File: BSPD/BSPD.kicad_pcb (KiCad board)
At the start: 2 copper layers, 81 x 61 mm, 31 parts, among them Q101 Q_PMOS_GSD, U101 641964-1, U102 641964-1, U103 R-78E5.0-0.5, U104 SN74LVC1G08DBVR, U105 LM339DR, U106 NE555DR, U107 SN74LVC3G14DCUR, U108 SN74AC32DR, U109 SN74LVC1G08DBVR, U110 641964-1

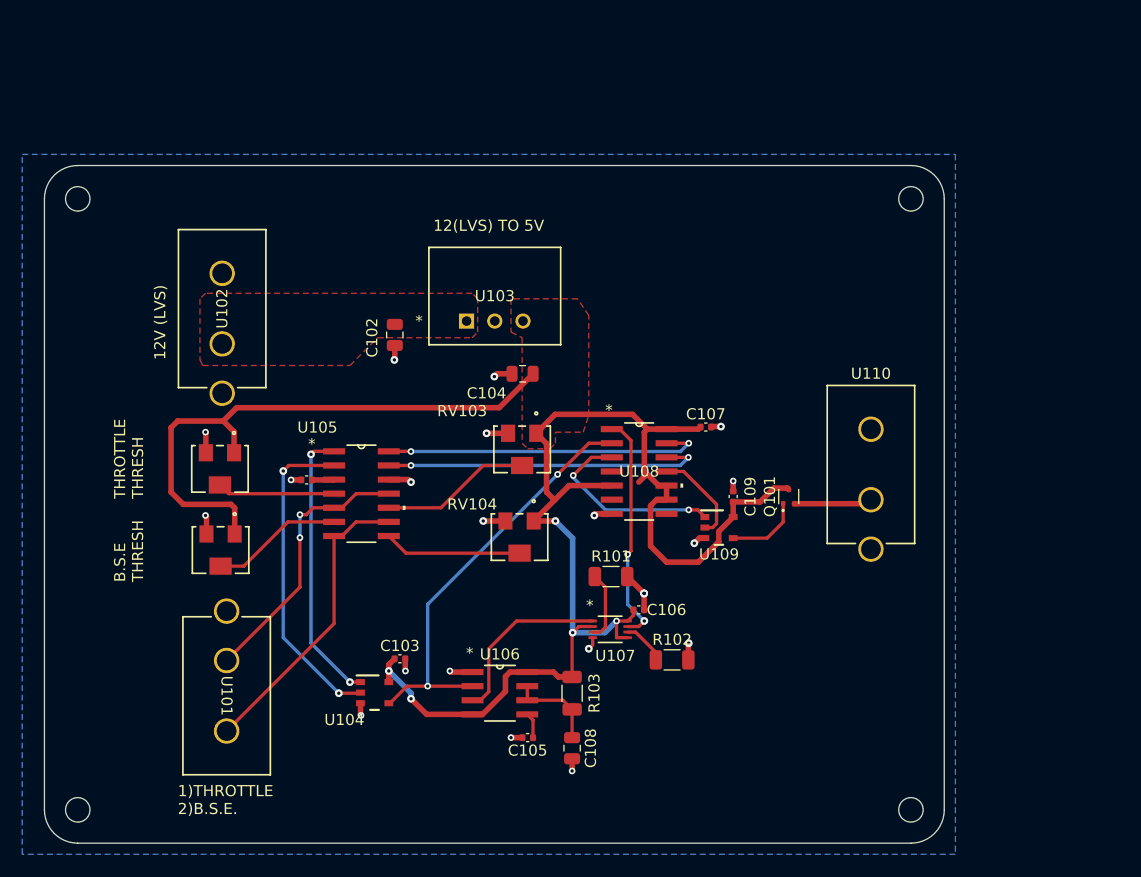
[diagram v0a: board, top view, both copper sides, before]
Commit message: resolved DRC errors for via sizes and footprints.
via size changed to 6mm/3mm should still work for JLC. Connected unconnected items. Changed footprints to fix overlap issue
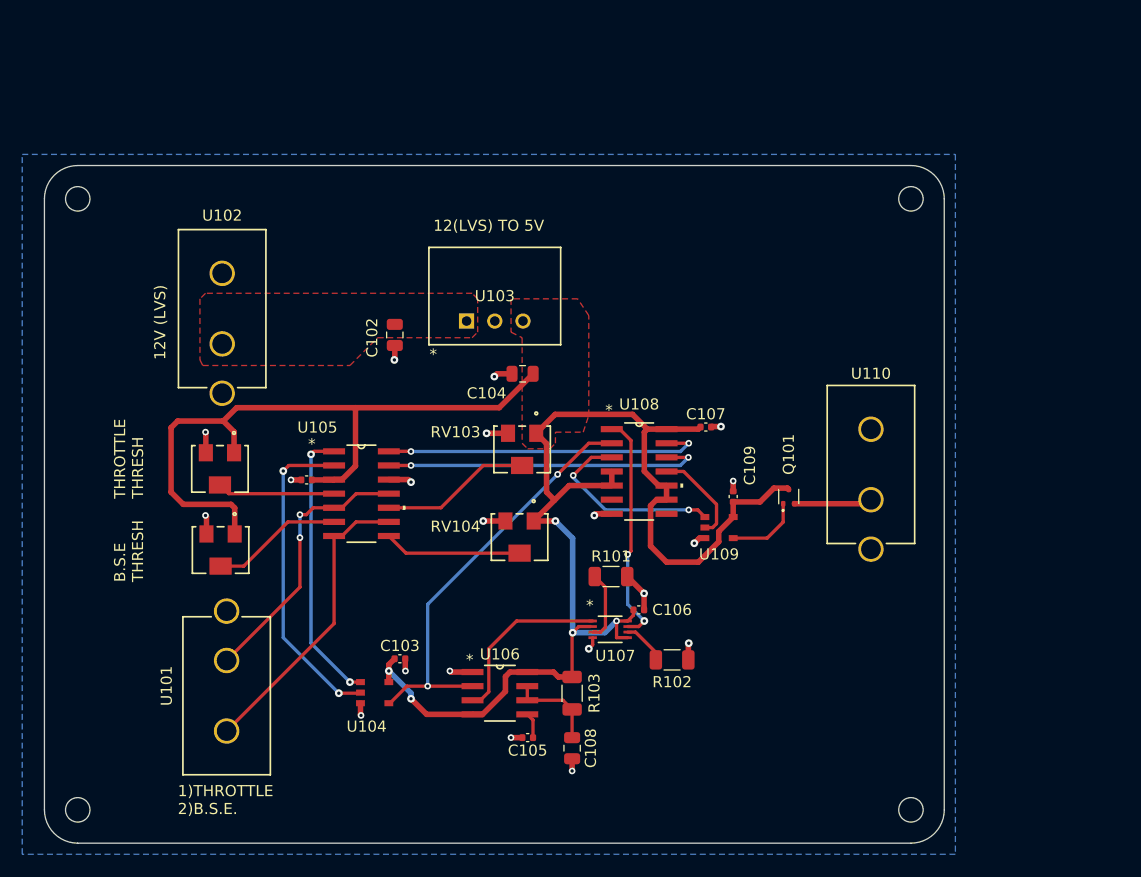
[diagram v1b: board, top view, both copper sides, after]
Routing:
- net +5V: track 167.8 -> 175.5 mm
- net GND: vias 21 -> 20
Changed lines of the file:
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@@
 		)
 		(fp_text user "*"
-			(at -2.7178 -3.6068 0)
-			(unlocked yes)
-			(layer "F.SilkS")
-			(effects
-				(font
-					(size 1 1)
-					(thickness 0.15)
-				)
-			)
-		)
-		(fp_text user "*"
-			(at -2.7178 -3.6068 0)
+			(at -2.7178 -3 0)
 			(layer "F.SilkS")
 			(effects
@@
 		(tags "SOT-523")
 		(property "Reference" "Q101"
-			(at 0 -1.7 90)
+			(at 3.8 0 90)
 			(layer "F.SilkS")
 			(effects
@@
 		(tags "641964-1 ")
 		(property "Reference" "U102"
-			(at 3.175 0 90)
+			(at 11.555 0 0)
 			(unlocked yes)
 			(layer "F.SilkS")
@@
 		(tags "3224W-1-103E ")
 		(property "Reference" "RV103"
-			(at 5.4 3.4522 0)
+			(at 6 1.5522 0)
 			(unlocked yes)
 			(layer "F.SilkS")
@@
 		(tags "resistor")
 		(property "Reference" "R102"
-			(at 0 -1.82 0)
+			(at 0 1.999999 0)
 			(layer "F.SilkS")
 			(effects
@@
 		(tags "capacitor")
 		(property "Reference" "C109"
-			(at 0 1.54 90)
+			(at 2.8 1.5 90)
 			(layer "F.SilkS")
 			(effects
@@
 		(tags "capacitor")
 		(property "Reference" "C106"
-			(at 2.5 0 0)
+			(at 3 0 0)
 			(layer "F.SilkS")
 			(effects
@@
 		(tags "SN74LVC1G08DBVR ")
 		(property "Reference" "U104"
-			(at -2.725001 2.449998 0)
+			(at -0.725001 3.049999 0)
 			(unlocked yes)
 			(layer "F.SilkS")
@@
 		(attr smd)
 		(fp_line
-			(start -1.625001 -1.549999)
-			(end 0.349999 -1.549999)
-			(stroke
-				(width 0.2)
-				(type solid)
-			)
-			(layer "F.SilkS")
-		)
-		(fp_line
-			(start -0.399999 1.549999)
-			(end 0.375003 1.549999)
-			(stroke
-				(width 0.2)
-				(type solid)
-			)
-			(layer "F.SilkS")
-		)
-		(fp_line
 			(start -1.750002 -1.650002)
 			(end 1.749999 -1.650002)
@@
 		)
 		(fp_line
-			(start -0.500002 0)
-			(end 0.499999 0)
-			(stroke
-				(width 0.1)
-				(type solid)
-			)
-			(layer "F.CrtYd")
-		)
-		(fp_line
-			(start 0 0.499999)
-			(end 0 -0.500002)
-			(stroke
-				(width 0.1)
-				(type solid)
-			)
-			(layer "F.CrtYd")
-		)
-		(fp_line
 			(start 1.749999 1.649999)
 			(end 1.749999 -1.650002)
@@
 		)
 		(fp_text user "*"
-			(at -4.2799 0 0)
-			(unlocked yes)
-			(layer "F.SilkS")
-			(effects
-				(font
-					(size 1 1)
-					(thickness 0.15)
-				)
-			)
-		)
-		(fp_text user "*"
-			(at -4.2799 0 0)
+			(at -3 3 0)
 			(layer "F.SilkS")
 			(effects
@@
 		(tags "SN74AC32DR ")
 		(property "Reference" "U108"
-			(at 0 0 0)
+			(at 0 -6.04 0)
 			(unlocked yes)
 			(layer "F.SilkS")
@@
 		(fp_text user "*"
 			(at -2.7178 -5.5118 0)
-			(layer "F.SilkS")
-			(effects
-				(font
-					(size 1 1)
-					(thickness 0.15)
-				)
-			)
-		)
-		(fp_text user "*"
-			(at -2.7178 -5.5118 0)
 			(unlocked yes)
 			(layer "F.SilkS")
@@
 		(tags "641964-1 ")
 		(property "Reference" "U101"
-			(at 3.175 0 270)
+			(at 2.286 5.4 90)
 			(unlocked yes)
 			(layer "F.SilkS")
@@
 		(attr smd)
 		(fp_line
-			(start -1.625001 -1.549999)
-			(end 0.349999 -1.549999)
-			(stroke
-				(width 0.2)
-				(type solid)
-			)
-			(layer "F.SilkS")
-		)
-		(fp_line
-			(start -0.399999 1.549999)
-			(end 0.375003 1.549999)
-			(stroke
-				(width 0.2)
-				(type solid)
-			)
-			(layer "F.SilkS")
-		)
-		(fp_line
 			(start -1.750002 -1.650002)
 			(end 1.749999 -1.650002)
@@
 		)
 		(fp_line
-			(start -0.500002 0)
-			(end 0.499999 0)
-			(stroke
-				(width 0.1)
-				(type solid)
-			)
-			(layer "F.CrtYd")
-		)
-		(fp_line
-			(start 0 0.499999)
-			(end 0 -0.500002)
-			(stroke
-				(width 0.1)
-				(type solid)
-			)
-			(layer "F.CrtYd")
-		)
-		(fp_line
 			(start 1.749999 1.649999)
 			(end 1.749999 -1.650002)
@@
 		)
 		(fp_text user "*"
-			(at -1.8288 -2.147 0)
-			(unlocked yes)
-			(layer "F.SilkS")
-			(effects
-				(font
-					(size 1 1)
-					(thickness 0.15)
-				)
-			)
-		)
-		(fp_text user "*"
 			(at -0.8128 -0.9779 0)
 			(layer "F.Fab")
@@
 		(tags "3224W-1-103E ")
 		(property "Reference" "RV104"
-			(at 4.27 2.9478 0)
+			(at 5.77 0.9478 0)
 			(unlocked yes)
 			(layer "F.SilkS")
@@
 	)
 	(via
-		(at 159.98 125.517501)
-		(size 0.7)
-		(drill 0.3)
-		(layers "F.Cu" "B.Cu")
-		(net 2)
-	)
-	(via
 		(at 164 130)
 		(size 0.7)
@@
 	)
 	(segment
+		(start 134 108.8)
+		(end 146.940068 108.8)
+		(width 0.5)
+		(layer "F.Cu")
+		(net 3)
+	)
+	(segment
 		(start 164.8662 110.73)
 		(end 165.0562 110.54)
@@
 	)
 	(segment
+		(start 157.0724 114.54)
+		(end 157.0724 115.81)
+		(width 0.5)
+		(layer "F.Cu")
+		(net 3)
+	)
+	(segment
 		(start 122.8 117.5)
 		(end 123.127597 117.827597)
@@
 	)
 	(segment
+		(start 134 114.0536)
+		(end 134 108.8)
+		(width 0.5)
+		(layer "F.Cu")
+		(net 3)
+	)
+	(segment
 		(start 117.4 116.4)
 		(end 118.5 117.5)
@@
 	)
 	(segment
-		(start 160 115)
-		(end 159.5 115.5)
-		(width 0.5)
-		(layer "F.Cu")
-		(net 3)
-	)
-	(segment
 		(start 132.0424 115.3)
 		(end 132.0724 115.27)
@@
 	)
 	(segment
+		(start 132.0724 115.27)
+		(end 132.7836 115.27)
+		(width 0.5)
+		(layer "F.Cu")
+		(net 3)
+	)
+	(segment
 		(start 147.5 134.3432)
 		(end 147.5 133)
@@
 	)
 	(segment
-		(start 160 114.5212)
-		(end 160 115)
-		(width 0.5)
-		(layer "F.Cu")
-		(net 3)
-	)
-	(segment
 		(start 117.4 110.6)
 		(end 117.4 116.4)
@@
 	)
 	(segment
+		(start 132.7836 115.27)
+		(end 134 114.0536)
+		(width 0.5)
+		(layer "F.Cu")
+		(net 3)
+	)
+	(segment
 		(start 160.27 110.73)
 		(end 162 110.73)
@@
 	(segment
 		(start 123.3 108.8)
-		(end 146.940068 108.8)
+		(end 134 108.8)
 		(width 0.5)
 		(layer "F.Cu")

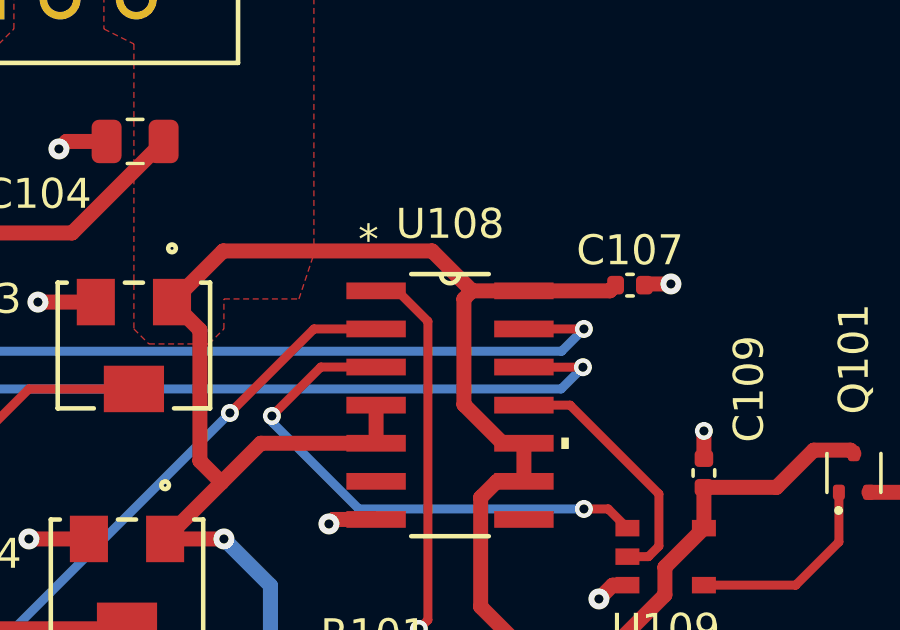
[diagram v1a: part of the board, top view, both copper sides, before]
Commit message: BSPD needs to be fixed + Fault Latch Layout Issue
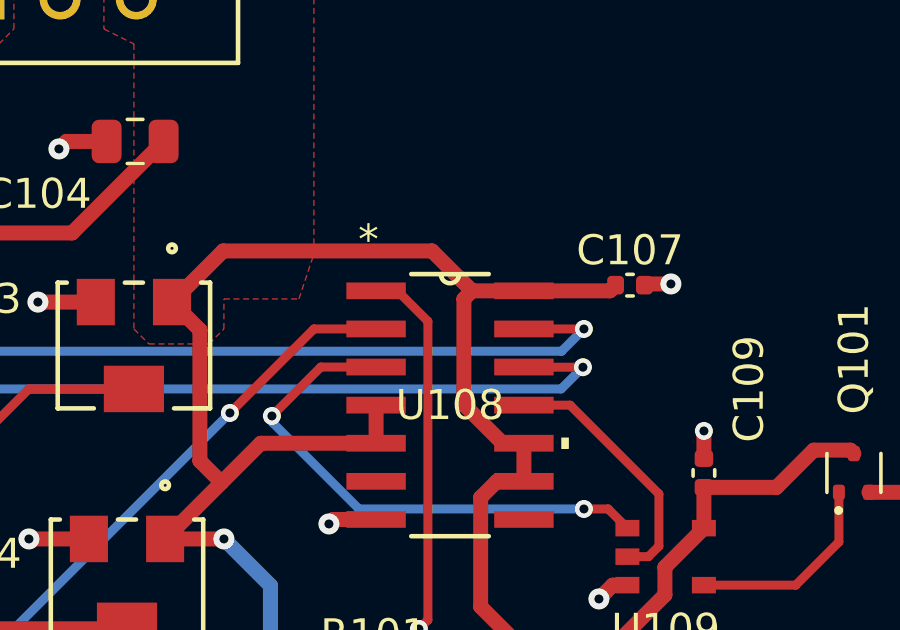
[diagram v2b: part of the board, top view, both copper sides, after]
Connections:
- Q101 pad 2: BSPD_TO_FAULT -> +5V
- Q101 pad 3: +5V -> BSPD_TO_FAULT
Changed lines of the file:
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@@
 			(layers "F.Cu" "F.Mask" "F.Paste")
 			(roundrect_rratio 0.25)
-			(net 6 "BSPD_TO_FAULT")
+			(net 3 "+5V")
 			(pinfunction "S")
 			(pintype "passive")
@@
 			(layers "F.Cu" "F.Mask" "F.Paste")
 			(roundrect_rratio 0.25)
-			(net 3 "+5V")
+			(net 6 "BSPD_TO_FAULT")
 			(pinfunction "D")
 			(pintype "passive")
@@
 		(tags "SN74AC32DR ")
 		(property "Reference" "U108"
-			(at 0 -6.04 0)
+			(at 0 0 0)
 			(unlocked yes)
 			(layer "F.SilkS")
@@
 		(fp_text user "*"
 			(at -2.7178 -5.5118 0)
-			(unlocked yes)
 			(layer "F.SilkS")
 			(effects
@@
 			(at -2.7178 -5.5118 0)
 			(unlocked yes)
-			(layer "F.Fab")
+			(layer "F.SilkS")
 			(effects
 				(font
@@
 			(unlocked yes)
 			(layer "F.Fab")
+			(effects
+				(font
+					(size 1 1)
+					(thickness 0.15)
+				)
+			)
+		)
+		(fp_text user "*"
+			(at -2.7178 -5.5118 0)
+			(unlocked yes)
+			(layer "F.Fab")

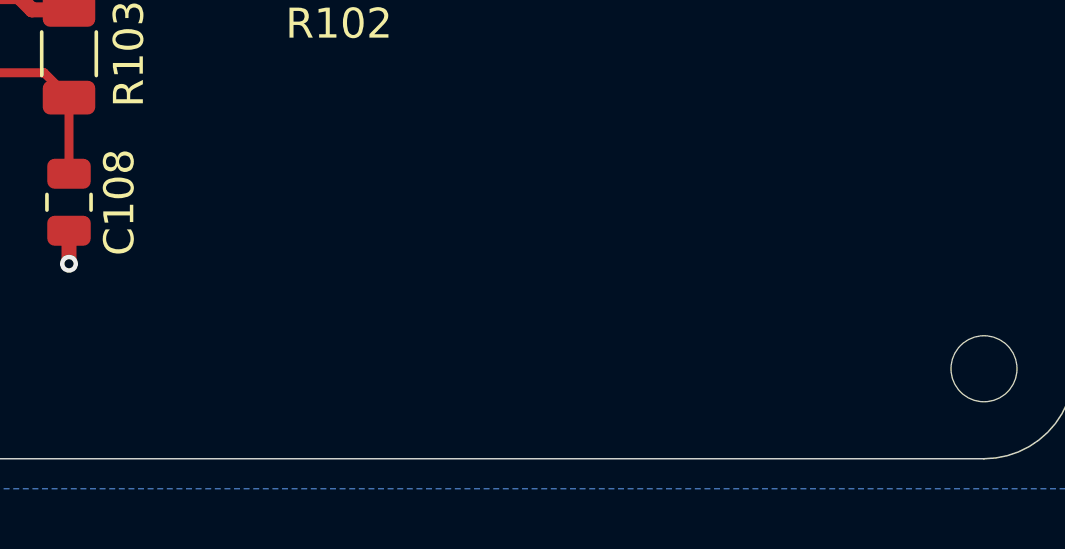
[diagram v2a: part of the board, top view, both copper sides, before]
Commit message: Fault latch added Logo
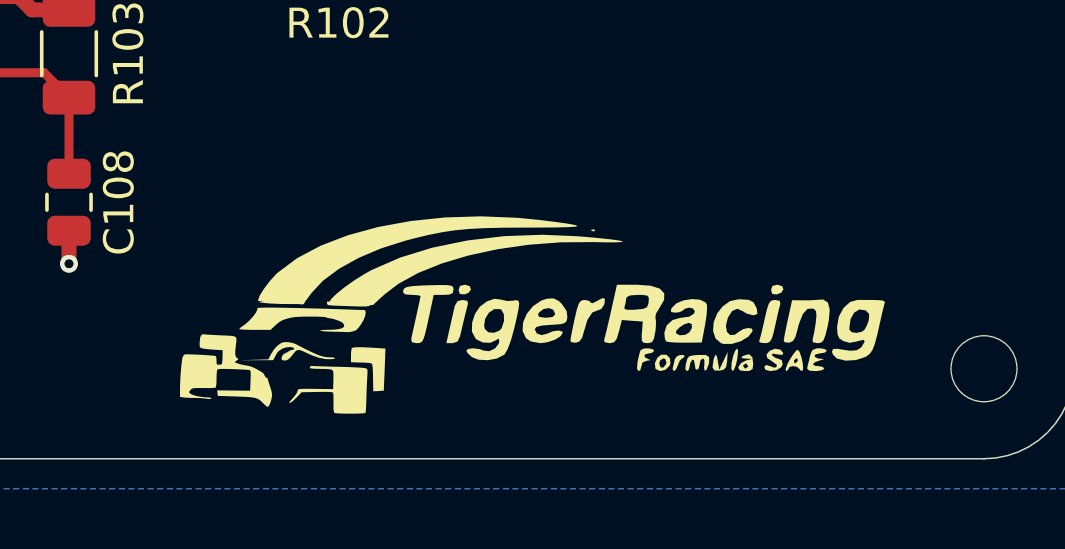
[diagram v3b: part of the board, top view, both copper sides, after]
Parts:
- added G***: LOGO, LOGO, F.Cu at (160.7, 144.7)
- added G***: LOGO, LOGO, F.Cu at (168.9, 143.3)

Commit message: BSPD READY
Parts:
- moved U107 18.9 mm to (171.6, 116.8)
- moved H101 18.9 mm to (123.7, 78.1)
- moved H102 18.9 mm to (123.7, 133.1)
- moved U104 18.9 mm to (150.4, 122.6)
- moved U109 18.9 mm to (181.4, 107.7)
- moved G*** 18.9 mm to (175.4, 132.8)
- moved RV102 18.9 mm to (136.5, 102.4)
- moved C105 18.9 mm to (164.2, 126.6)
- moved G*** 18.9 mm to (183.6, 131.4)
- moved H103 18.9 mm to (198.7, 133.1)
- moved H104 18.9 mm to (198.7, 78.1)
- moved R103 18.9 mm to (168.2, 122.6)
- moved RV101 18.9 mm to (136.6, 109.7)
- moved RV104 18.9 mm to (163.5, 108.5)
- moved U102 18.9 mm to (136.7, 91.2)
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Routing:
- net 2OUT: track 28.8 -> 85.9 mm, vias 2 -> 0
- net 1OUT: track 25.1 -> 74.9 mm, vias 2 -> 0
- net +5V: track 175.5 -> 224.1 mm, vias 5 -> 2
- net GND: track 30.8 -> 2.36 mm, vias 20 -> 289
- net THRESH_BSE: track 11.9 -> 37.8 mm
- net Net-(U108-1Y): track 17.7 -> 28.4 mm
- net BSE_IN: track 27.0 -> 17.3 mm
- net THRESH_THROTTLE: track 10.6 -> 14.2 mm
- net 3OUT: track 29.3 -> 31.9 mm, vias 2 -> 0
- net 4OUT: track 29.2 -> 31.6 mm, vias 2 -> 0
- net Net-(Q101-G): track 6.75 -> 5.23 mm
- net THROTTLE_IN: track 24.6 -> 23.2 mm, vias 2 -> 0
- net Net-(U104-Y): track 38.1 -> 39.5 mm, vias 2 -> 0
- net Net-(U106-OUT): track 16.7 -> 15.4 mm
- net BSPD_TO_FAULT: track 7.05 -> 8.05 mm
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- added copper zone on F.Cu, net GND
- removed copper zone on F.Cu, net +5V

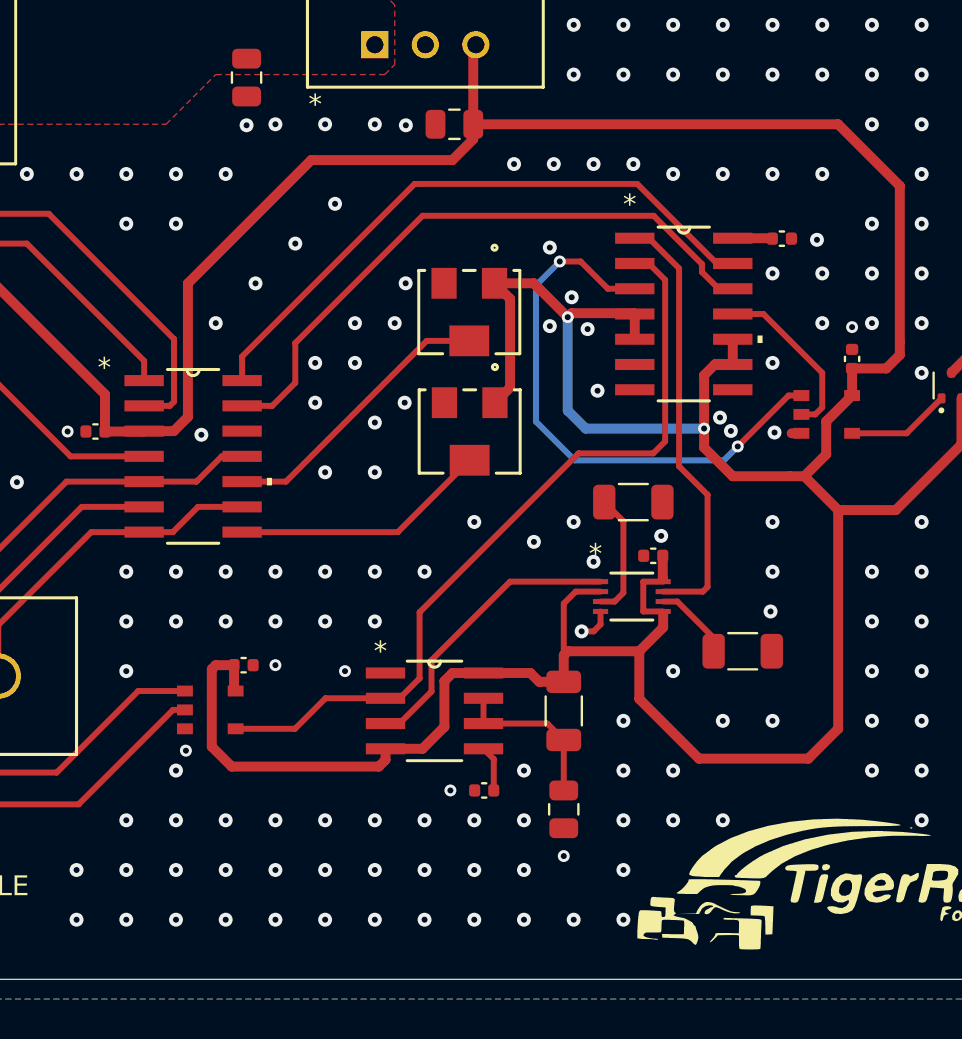
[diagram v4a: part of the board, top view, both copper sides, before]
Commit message: Double checked PMOS output logic. Added connector and routing for sense wires from sensors. Connected one unconnected track. 2 DRC errors about spokes, but otherwise Ready to Geaux :3
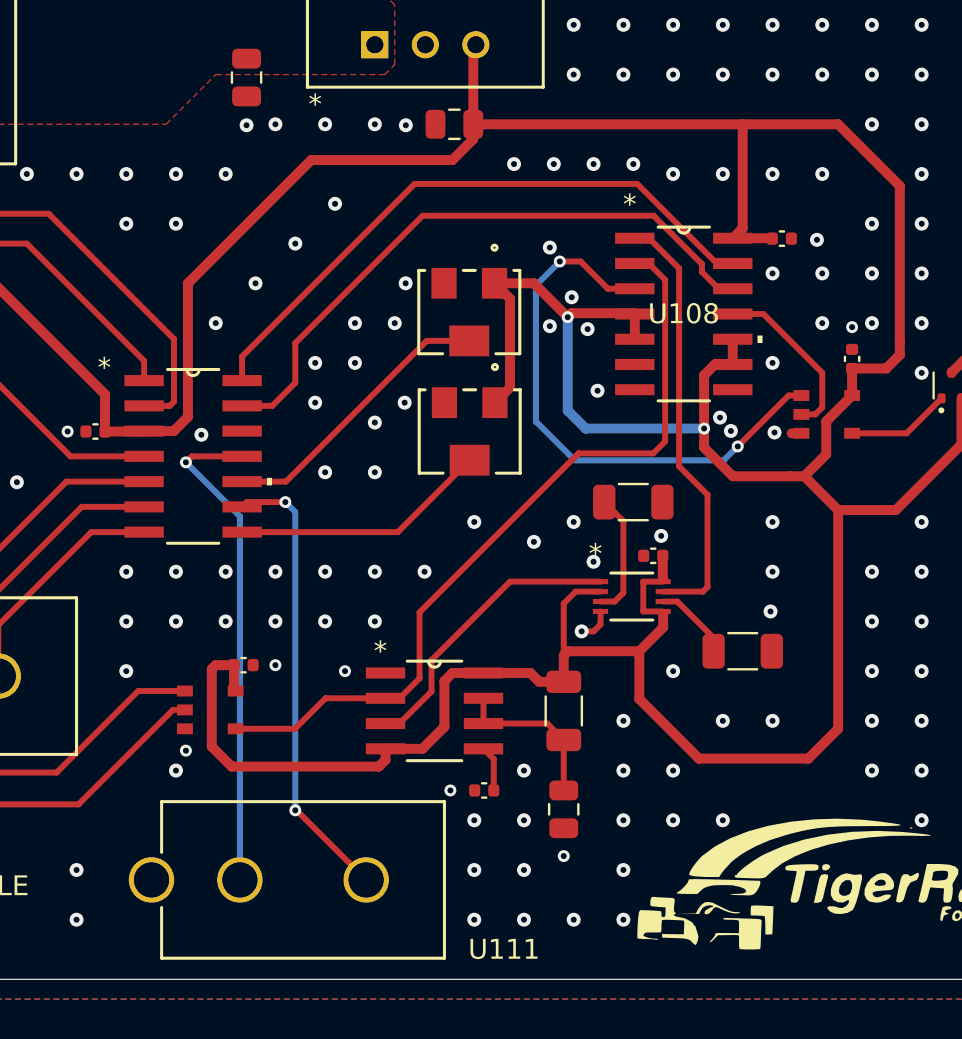
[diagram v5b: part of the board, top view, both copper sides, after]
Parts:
- added U111: 641964-1, 641964-1:641964-1_TYC, F.Cu at (151.9, 131.1)
- U108: footprint SN74AC32DR:D14 -> LM339DR:D14
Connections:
- U105 pad 11: THROTTLE_IN -> THROTTLE_Sense_IN
- U105 pad 9: BSE_IN -> BSE_Sense_IN
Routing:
- net THROTTLE_Sense_IN: track 0.00 -> 25.1 mm, vias 0 -> 1
- net BSE_Sense_IN: track 0.00 -> 23.0 mm, vias 0 -> 2
- net +5V: track 224.1 -> 230.1 mm
- net THROTTLE_IN: track 23.2 -> 17.7 mm
- net BSE_IN: track 17.3 -> 11.8 mm
- net GND: vias 289 -> 268
